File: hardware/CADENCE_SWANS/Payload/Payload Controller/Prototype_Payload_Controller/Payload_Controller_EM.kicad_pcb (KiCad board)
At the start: 2 copper layers, 100 x 100 mm, 122 parts, among them J1 Conn_01x06_Pin, J11 Conn_01x04, J12 Conn_01x02, J13 USB_C_Receptacle_USB2.0_16P, J14 Conn_01x02, J15 Conn_02x02_Top_Bottom, J2 Conn_01x06_Pin, J3 Conn_01x06_Pin, J4 Conn_01x06_Pin, J5 Conn_Coaxial, J6 Conn_Coaxial, J7 Conn_Coaxial, J8 Conn_Coaxial, J9 Conn_01x02, SW1 KMR2, SW2 KMR2, U1 SN65C1168ERGYR, U25 LSM6DSO, U27 LIS2MDL, U28 INA219AxDCN, U29 TMP112xxDRL, U3 LT8612, U5 LT8612, U6 LT8612, U8 ATSAMV71Q21B-A, Y1 ABM3B-12.000MHZ-B2-T, Y2 ABS07-32.768KHZ-T

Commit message: changed to 4 layer board
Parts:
- moved U8 2.57 mm to (158.3, 49.8)
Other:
- copper layers 2 -> 4
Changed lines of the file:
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@@
 	(layers
 		(0 "F.Cu" signal)
+		(4 "In1.Cu" signal)
+		(6 "In2.Cu" signal)
 		(2 "B.Cu" signal)
 		(9 "F.Adhes" user "F.Adhesive")
@@
 	)
 	(setup
+		(stackup
+			(layer "F.SilkS"
+				(type "Top Silk Screen")
+			)
+			(layer "F.Paste"
+				(type "Top Solder Paste")
+			)
+			(layer "F.Mask"
+				(type "Top Solder Mask")
+				(thickness 0.01)
+			)
+			(layer "F.Cu"
+				(type "copper")
+				(thickness 0.035)
+			)
+			(layer "dielectric 1"
+				(type "prepreg")
+				(thickness 0.1)
+				(material "FR4")
+				(epsilon_r 4.5)
+				(loss_tangent 0.02)
+			)
+			(layer "In1.Cu"
+				(type "copper")
+				(thickness 0.035)
+			)
+			(layer "dielectric 2"
+				(type "core")
+				(thickness 1.24)
+				(material "FR4")
+				(epsilon_r 4.5)
+				(loss_tangent 0.02)
+			)
+			(layer "In2.Cu"
+				(type "copper")
+				(thickness 0.035)
+			)
+			(layer "dielectric 3"
+				(type "prepreg")
+				(thickness 0.1)
+				(material "FR4")
+				(epsilon_r 4.5)
+				(loss_tangent 0.02)
+			)
+			(layer "B.Cu"
+				(type "copper")
+				(thickness 0.035)
+			)
+			(layer "B.Mask"
+				(type "Bottom Solder Mask")
+				(thickness 0.01)
+			)
+			(layer "B.Paste"
+				(type "Bottom Solder Paste")
+			)
+			(layer "B.SilkS"
+				(type "Bottom Silk Screen")
+			)
+			(copper_finish "None")
+			(dielectric_constraints no)
+		)
 		(pad_to_mask_clearance 0)
 		(allow_soldermask_bridges_in_footprints no)
@@
 	(footprint "Package_QFP:LQFP-144_20x20mm_P0.5mm"
 		(layer "F.Cu")
-		(at 158.0234 52.3632)
+		(at 158.2983 49.8096)
 		(descr "LQFP, 144 Pin (http://ww1.microchip.com/downloads/en/PackagingSpec/00000049BQ.pdf#page=425), generated with kicad-footprint-generator ipc_gullwing_generator.py")
 		(tags "LQFP QFP")

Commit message: resolved ERC errors
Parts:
- L1, L3, L4: footprint Footprints:IND-SMD_L10.9-W10.0 -> Inductor_SMD:L_6.3x6.3_H3
- moved C2 94.0 mm to (261.0, 51.5)
- moved C3 94.0 mm to (242.3, 51.5)
- moved C36 94.0 mm to (246.9, 38.0)
- moved C37 94.0 mm to (246.9, 39.9)
- moved C4 94.0 mm to (242.3, 54.0)
- moved J11 94.0 mm to (237.4, 37.3)
- moved J13 94.0 mm to (254.2, 40.8)
- moved R1 94.0 mm to (261.0, 54.0)
- moved SW1 94.0 mm to (263.1, 37.1)
- moved SW2 94.0 mm to (263.1, 41.4)
- moved C13 94.0 mm to (241.2, 39.9)
- moved C23 94.0 mm to (241.2, 41.9)
- moved C26 94.0 mm to (241.2, 43.9)
- moved C27 94.0 mm to (241.2, 45.8)
- moved C29 94.0 mm to (244.1, 38.0)
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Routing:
- added copper zone on B.Cu, net +3V3
- added copper zone on F.Cu, net GND
- added copper zone on In1.Cu, net GND

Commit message: layout updates
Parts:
- added C4: 100nF, Capacitor_SMD:C_0603_1608Metric, F.Cu at (157.2, 135.9)
- added R1: 0.002, Resistor_SMD:R_0402_1005Metric, F.Cu at (169.5, 140.0)
- added U1: INA219AxDCN, Package_TO_SOT_SMD:SOT-23-8, F.Cu at (166.6, 136.8)
- J10: renamed from J7; moved to B.Cu
- J11: renamed from J6; moved to B.Cu
- J12: renamed from J8; moved to B.Cu
- J5: renamed from J1; moved to B.Cu
- J6: renamed from J3; moved to B.Cu
- J7: renamed from J2; moved to B.Cu
- J8: renamed from J4; moved to B.Cu
- J9: renamed from J5; moved to B.Cu
- U6: renamed from U2; moved to B.Cu
- U8: renamed from U4; moved to B.Cu
- moved C43 158.6 mm to (153.2, 159.0)
- moved C15 121.5 mm to (207.8, 141.9)
- moved C10 121.4 mm to (207.8, 137.3)
- moved C11 121.4 mm to (207.8, 139.8)
- moved C21 121.4 mm to (220.1, 135.0)
- moved C22 121.4 mm to (220.1, 138.0)
- moved C3 121.4 mm to (215.9, 134.8)
- moved C7 121.4 mm to (220.1, 141.0)
- moved C8 121.4 mm to (220.1, 144.1)
- moved C9 121.4 mm to (207.8, 134.8)
- moved R11 121.4 mm to (215.9, 137.3)
- moved R4 121.4 mm to (215.9, 139.8)
- moved C1 121.4 mm to (211.8, 144.8)
- moved C12 121.4 mm to (211.8, 139.8)
- moved C13 121.4 mm to (223.7, 134.5)
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- renumbered C46 to C1, C8 to C10, C9 to C11, C39 to C12, C40 to C13, C41 to C14, C19 to C16, C20 to C17, C24 to C18, C42 to C19, C47 to C2, C43 to C20, C44 to C21, C45 to C22, C27 to C23, C35 to C24, C38 to C25, C14 to C26, C28 to C27, C17 to C28, C48 to C3, C18 to C30, C30 to C31, C37 to C32, C23 to C33, C5 to C34, C6 to C35, C13 to C36, C36 to C37, C31 to C38, C26 to C39, C32 to C40, C33 to C41, C34 to C42, C1 to C43, C2 to C44, C4 to C45, C3 to C46, C99 to C47, C103 to C48, C100 to C49, C49 to C5, C101 to C50, C50 to C6, C51 to C7, C52 to C8, C7 to C9, D7 to D1, D6 to D2, D5 to D3, J13 to J1, J15 to J13, J9 to J14, J12 to J2, J11 to J3, J14 to J4, L4 to L1, L1 to L2, R23 to R10, R24 to R11, R25 to R12, R22 to R13, R17 to R14, R16 to R15, R18 to R16, R19 to R17, R14 to R18, R15 to R19, R26 to R2, R12 to R21, R21 to R22, R13 to R23, R1 to R24, R27 to R3, R28 to R4, R29 to R5, R5 to R6, R11 to R7, R6 to R8, R7 to R9, TP5 to TP1, TP8 to TP10, TP2 to TP11, TP1 to TP12, TP3 to TP13, TP4 to TP2, TP11 to TP3, TP10 to TP4, TP6 to TP5, TP7 to TP6, TP13 to TP7, TP9 to TP8, TP12 to TP9, U25 to U10, U27 to U11, U5 to U2, U6 to U3, U3 to U4, U8 to U5, U1 to U7, U29 to U9
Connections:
- C43 pad 1: VDD -> +12V
- D3 pad 2: +3V3 -> +3.3V
- J5 pad 1: VDD -> +12V
- J6 pad 1: VDD -> +12V
- J7 pad 1: VDD -> +12V
- J8 pad 1: VDD -> +12V
- U5 pad 8: unconnected-(U8-VREFN-Pad8) -> GND
- U5 pad 9: unconnected-(U8-VREFP-Pad9) -> +3V3
- U6 pad 1: VDD -> +12V
- U8 pad 1: (no net) -> unconnected-(U8E-DC-Pad1)
- U8 pad 21: (no net) -> unconnected-(U8E-DC-Pad21)
- U8 pad 22: (no net) -> unconnected-(U8E-DC-Pad22)
- U8 pad 24: (no net) -> unconnected-(U8E-DC-Pad24)
- U8 pad 30: (no net) -> unconnected-(U8E-DC-Pad30)
- U8 pad 42: (no net) -> unconnected-(U8E-DC-Pad42)
- U8 pad 44: (no net) -> unconnected-(U8E-DC-Pad44)
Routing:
- net +3V3: track 0.00 -> 6.57 mm
- net GND: track 0.00 -> 5.30 mm, vias 0 -> 5
- net +1V2: track 0.00 -> 5.12 mm

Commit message: layout updates
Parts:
- J5: renamed from J9; footprint Connector_Coaxial:SMA_Amphenol_901-144_Vertical -> Connector_Coaxial:MMCX_Molex_73415-1471_Vertical; moved to F.Cu
- J6: renamed from J11; footprint Connector_Coaxial:SMA_Amphenol_901-144_Vertical -> Connector_Coaxial:MMCX_Molex_73415-1471_Vertical; moved to F.Cu
- J7: renamed from J10; footprint Connector_Coaxial:SMA_Amphenol_901-144_Vertical -> Connector_Coaxial:MMCX_Molex_73415-1471_Vertical; moved to F.Cu
- J8: renamed from J12; footprint Connector_Coaxial:SMA_Amphenol_901-144_Vertical -> Connector_Coaxial:MMCX_Molex_73415-1471_Vertical; moved to F.Cu
- U4: renamed from U8; moved to F.Cu
- moved J8 72.3 mm to (162.2, 64.8), turned to -45 degrees
- moved J15 66.1 mm to (119.2, 75.5), turned to -45 degrees
- moved J6 64.6 mm to (169.4, 71.8), turned to -45 degrees
- moved J7 64.3 mm to (158.8, 61.4), turned to 45 degrees
- moved R15 61.5 mm to (183.6, 90.5), turned to 180 degrees
- moved R18 59.9 mm to (188.5, 93.8), turned to 90 degrees
- moved R19 53.6 mm to (188.5, 89.2), turned to 90 degrees
- moved J5 52.6 mm to (165.8, 68.3), turned to 135 degrees
- moved R14 52.1 mm to (183.6, 91.9)
- moved U1 42.7 mm to (132.5, 63.9), turned to 135 degrees
- moved U6 36.7 mm to (179.5, 152.9)
- moved U3 35.9 mm to (167.3, 115.4)
- moved U5 35.9 mm to (176.0, 115.3)
- moved C38 29.0 mm to (164.1, 79.3), turned to -45 degrees
- moved C32 28.8 mm to (163.1, 77.3), turned to 45 degrees
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- renumbered C43 to C1, C49 to C100, C50 to C101, C48 to C103, C4 to C105, C36 to C13, C26 to C14, C28 to C17, C30 to C18, C16 to C19, C44 to C2, C17 to C20, C33 to C23, C18 to C24, C39 to C26, C23 to C27, C27 to C28, C46 to C3, C31 to C30, C38 to C31, C40 to C32, C41 to C33, C42 to C34, C24 to C35, C37 to C36, C32 to C37, C25 to C38, C12 to C39, C45 to C4, C13 to C40, C14 to C41, C19 to C42, C20 to C43, C21 to C44, C22 to C45, C1 to C46, C2 to C47, C3 to C48, C5 to C49, C34 to C5, C6 to C50, C7 to C51, C8 to C52, C35 to C6, C9 to C7, C10 to C8, C11 to C9, C47 to C99, D3 to D5, D2 to D6, D1 to D7, J5 to J1, J3 to J11, J2 to J12, J1 to J13, J4 to J14, J13 to J15, J7 to J2, J6 to J3, J8 to J4, J14 to J9, L2 to L1, L1 to L4, R24 to R1, R7 to R11, R21 to R12, R1 to R121, R23 to R13, R18 to R14, R19 to R15, R15 to R16, R14 to R17, R16 to R18, R17 to R19, R22 to R21, R13 to R22, R10 to R23, R11 to R24, R12 to R25, R2 to R26, R3 to R27, R4 to R28, R5 to R29, R6 to R5, R8 to R6, R9 to R7, TP12 to TP1, TP4 to TP10, TP3 to TP11, TP9 to TP12, TP7 to TP13, TP11 to TP2, TP13 to TP3, TP2 to TP4, TP1 to TP5, TP5 to TP6, TP6 to TP7, TP10 to TP8, TP8 to TP9, U7 to U1, U6 to U2, U10 to U25, U11 to U27, U9 to U29, U4 to U3, U1 to U31, U2 to U5, U3 to U6, U5 to U8
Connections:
- net Net-(J1-D+-PadA6) renamed /Microcontroller/D+
- net Net-(J1-D--PadA7) renamed /Microcontroller/D-
- C38 pad 1: +3V3 -> +1V2
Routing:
- net +1V2: track 5.12 -> 85.1 mm
- net /MRAM/A9: track 0.00 -> 40.2 mm, vias 0 -> 2
- net /MRAM/MRAM_DATA0: track 0.00 -> 35.5 mm, vias 0 -> 2
- net GND: track 5.30 -> 36.9 mm, vias 5 -> 23
- net /Microcontroller/USB_D-: track 0.00 -> 25.2 mm
- net /Microcontroller/USB_D+: track 0.00 -> 24.8 mm
- net +3V3: track 6.57 -> 24.0 mm, vias 0 -> 6
- net /Instrument/RADFET_OUT2: track 0.00 -> 14.4 mm
- net /Instrument/RADFET_OUT3: track 0.00 -> 13.1 mm
- net /Microcontroller/D+: track 0.00 -> 11.8 mm, vias 0 -> 2
- net /Instrument/RADFET_OUT1: track 0.00 -> 11.6 mm
- net /Instrument/RADFET_OUT4: track 0.00 -> 11.4 mm
- net /Microcontroller/D-: track 0.00 -> 7.77 mm
- net /Microcontroller/XOUT: track 0.00 -> 7.36 mm
- net /Microcontroller/XIN: track 0.00 -> 6.92 mm
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- added copper zone on In2.Cu, net +3V3
- added copper zone on B.Cu, net GND
- removed copper zone on B.Cu, net +3V3

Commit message: updates
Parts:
- moved U1 49.2 mm to (106.5, 105.7), turned to -45 degrees
- moved U4 38.7 mm to (130.2, 62.6), turned to 135 degrees
- moved J7 25.9 mm to (184.4, 57.8)
- moved J8 25.9 mm to (187.8, 61.3)
- moved J5 25.9 mm to (191.5, 64.7)
- moved J6 25.9 mm to (195.1, 68.3)
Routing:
- net /MRAM/A9: track 40.2 -> 2.02 mm, vias 2 -> 1
- net /MRAM/MRAM_DATA0: track 35.5 -> 1.42 mm, vias 2 -> 1
- net /Instrument/RADFET_OUT2: track 14.4 -> 0.00 mm
- net /Instrument/RADFET_OUT3: track 13.1 -> 0.00 mm
- net /Instrument/RADFET_OUT1: track 11.6 -> 0.00 mm
- net /Instrument/RADFET_OUT4: track 11.4 -> 0.00 mm
- net +1V2: track 85.1 -> 84.5 mm

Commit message: layout changes
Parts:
- J1, J2, J3, U2: moved to F.Cu
- moved U2 70.8 mm to (58.6, 42.7), turned to -45 degrees
- moved U4 47.4 mm to (148.0, 106.5), turned to 90 degrees
- moved J3 31.4 mm to (145.6, 36.8)
- moved J14 12.7 mm to (221.3, 73.7)
- moved J12 12.7 mm to (216.6, 73.7)
- moved J2 8.98 mm to (180.2, 39.6)
- moved J1 7.59 mm to (169.8, 43.0), turned to 180 degrees
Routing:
- net /MRAM/MRAM_DATA4: track 0.00 -> 60.3 mm, vias 0 -> 2
- net /MRAM/A20: track 0.00 -> 49.1 mm
- net /MRAM/MRAM_DATA5: track 0.00 -> 47.5 mm, vias 0 -> 2
- net /MRAM/MRAM_DATA6: track 0.00 -> 45.3 mm, vias 0 -> 2
- net /MRAM/A8: track 1.56 -> 42.8 mm, vias 1 -> 2
- net /MRAM/MRAM_DATA7: track 0.00 -> 39.8 mm, vias 0 -> 2
- net /MRAM/A9: track 2.02 -> 41.0 mm, vias 1 -> 2
- net /MRAM/A19: track 0.00 -> 37.2 mm, vias 0 -> 2
- net /MRAM/A14: track 0.00 -> 36.6 mm, vias 0 -> 2
- net /MRAM/A15: track 0.00 -> 36.3 mm, vias 0 -> 2
- net /MRAM/A6: track 0.00 -> 34.9 mm, vias 0 -> 2
- net /MRAM/A16: track 0.00 -> 32.6 mm, vias 0 -> 2
- net /MRAM/A3: track 0.00 -> 31.6 mm
- net /MRAM/A2: track 0.00 -> 31.2 mm
- net /MRAM/A0: track 0.00 -> 30.7 mm
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
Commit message: MRAM Layout
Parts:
- moved C2 137.2 mm to (123.9, 53.2)
- moved R1 137.2 mm to (123.9, 55.7)
- moved TP1 137.2 mm to (120.3, 53.5)
- moved TP2 137.2 mm to (120.3, 56.5)
- moved TP3 137.2 mm to (120.3, 59.6)
- moved J12 109.2 mm to (109.1, 92.7)
- moved J14 109.2 mm to (113.8, 92.7)
- moved U1 47.7 mm to (133.0, 66.1)
- moved J15 6.86 mm to (125.2, 72.1)
- moved C23 1.62 mm to (140.8, 94.1)
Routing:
- net /MRAM/MRAM_DATA1: track 0.00 -> 63.1 mm, vias 0 -> 2
- net /MRAM/MRAM_DATA0: track 0.00 -> 60.1 mm, vias 0 -> 2
- net /MRAM/MRAM_CTRL.WE: track 2.36 -> 45.6 mm, vias 1 -> 2
- net /MRAM/A5: track 0.00 -> 26.5 mm
- net /Microcontroller/URXD2: track 0.00 -> 17.0 mm
- net /Microcontroller/UTXD2: track 0.00 -> 9.65 mm
- net +3V3: track 24.0 -> 32.2 mm, vias 6 -> 7
- net GND: track 38.7 -> 44.3 mm, vias 24 -> 25
- net /MRAM/MRAM_CTRL.CS: track 0.00 -> 2.38 mm, vias 0 -> 1
- net /MRAM/MRAM_CTRL.OE: track 14.4 -> 15.2 mm

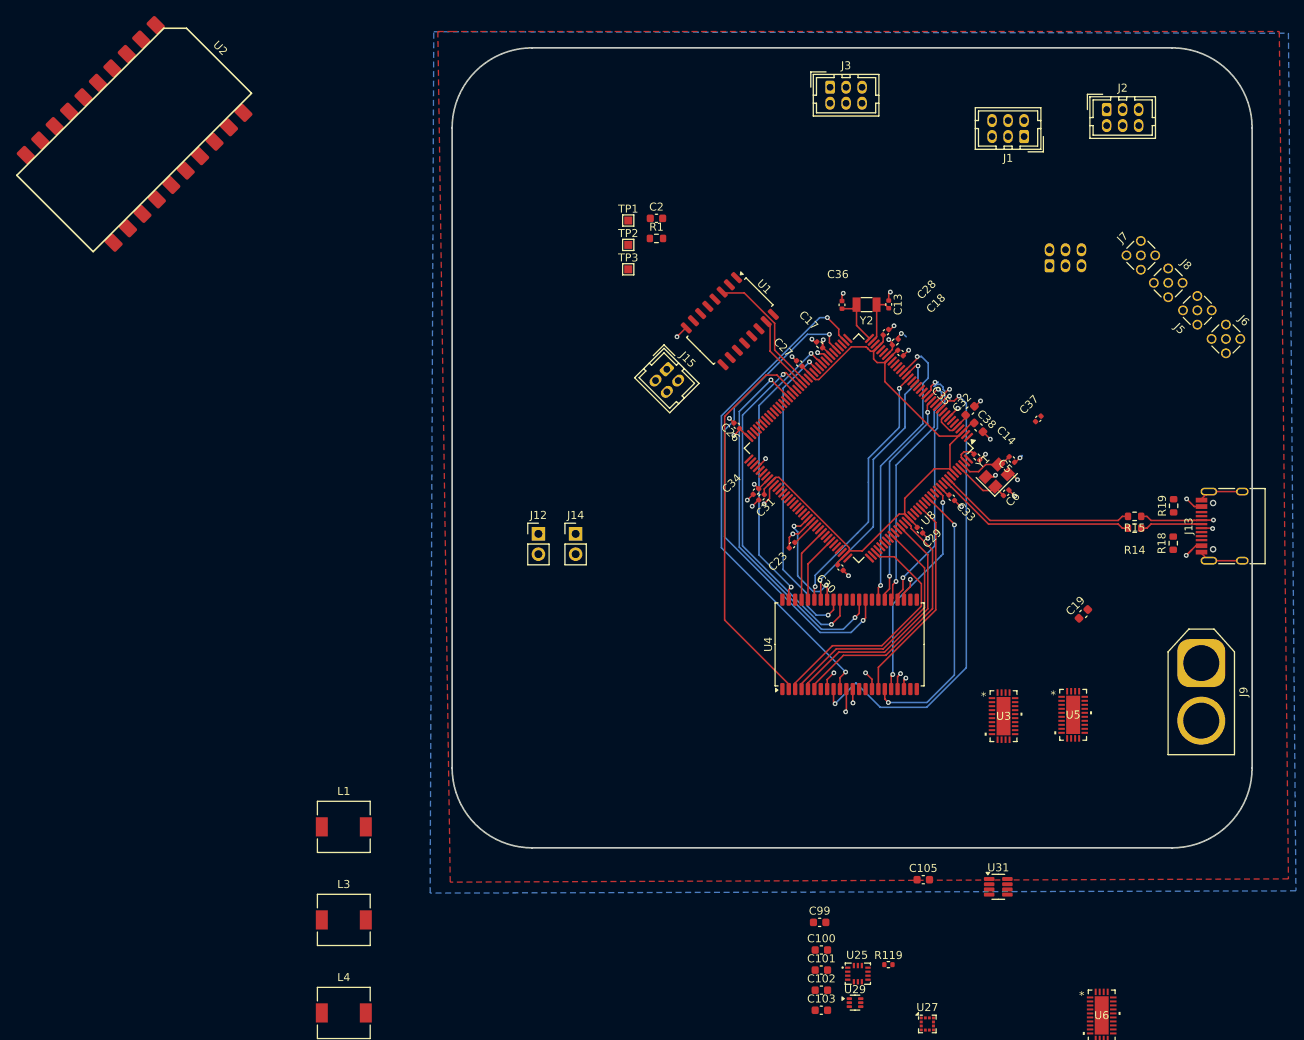
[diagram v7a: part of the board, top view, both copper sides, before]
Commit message: routed RS422 differential traces
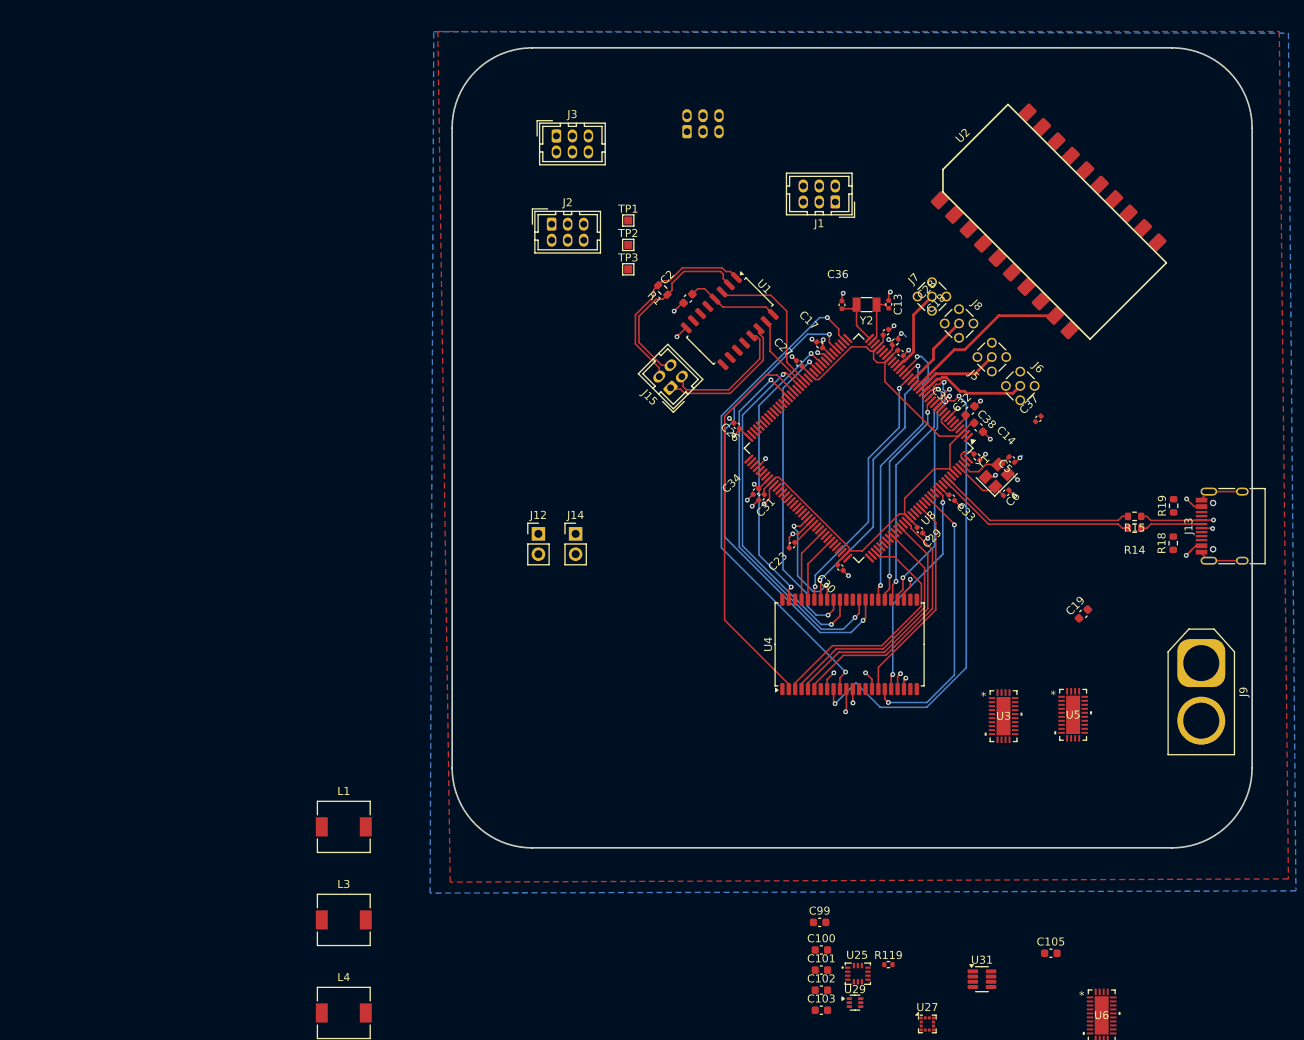
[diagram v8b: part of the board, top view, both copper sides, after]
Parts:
- moved U2 114.9 mm to (172.9, 53.7), turned to 45 degrees
- moved J2 70.8 mm to (110.8, 53.9)
- moved J4 48.3 mm to (127.7, 42.4)
- moved J3 34.7 mm to (111.4, 42.9)
- moved J8 26.6 mm to (161.7, 66.4)
- moved J7 26.6 mm to (158.3, 63.0)
- moved J6 26.4 mm to (169.3, 74.2)
- moved J5 26.3 mm to (165.8, 70.6)
- moved J1 25.0 mm to (146.2, 51.2)
- moved C105 18.4 mm to (173.2, 145.1)
- moved U31 11.7 mm to (164.6, 148.3)
- moved C2 10.8 mm to (127.8, 63.2), turned to -135 degrees
- moved R1 6.49 mm to (124.7, 62.2), turned to 135 degrees
- moved J15 2.37 mm to (125.6, 74.4), turned to 135 degrees
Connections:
- J15 pad 1: /Flight Computer Interface/Payload_TX+ -> /Flight Computer Interface/Payload_TX-
- J15 pad 2: /Flight Computer Interface/Payload_TX- -> /Flight Computer Interface/Payload_TX+
- J15 pad 3: /Flight Computer Interface/Payload_RX+ -> /Flight Computer Interface/Payload_RX-
- J15 pad 4: /Flight Computer Interface/Payload_RX- -> /Flight Computer Interface/Payload_RX+
- U8 pad 25: unconnected-(U8-PA17-Pad25) -> /Microcontroller/AFE0_AD6
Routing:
- net /Flight Computer Interface/Payload_RX-: track 0.00 -> 25.0 mm
- net /Flight Computer Interface/Payload_RX+: track 0.00 -> 23.5 mm
- net /Instrument/RADFET_OUT0: track 0.00 -> 20.9 mm
- net /Flight Computer Interface/Payload_TX-: track 0.00 -> 17.8 mm
- net /Flight Computer Interface/Payload_TX+: track 0.00 -> 16.3 mm
- net /Instrument/RADFET_OUT2: track 0.00 -> 14.1 mm
- net +5V: track 0.00 -> 11.7 mm
- net /Instrument/RADFET_OUT3: track 0.00 -> 10.6 mm
- net /Instrument/RADFET_OUT1: track 0.00 -> 10.6 mm
- net /Instrument/RADFET_OUT4: track 0.00 -> 9.61 mm
- net /Microcontroller/URXD2: track 17.0 -> 18.7 mm
- net GND: track 44.3 -> 45.9 mm, vias 25 -> 26
- net /MRAM/A11: track 33.6 -> 32.8 mm
